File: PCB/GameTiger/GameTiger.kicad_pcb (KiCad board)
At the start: 2 copper layers, 81.3 x 99.8 mm, 79 parts, among them J1 USB TypeC Connector, J2 503398-1892, J3 LCD Display, J4 Speaker, Q1 DMG3415, U1 RP2040, U2 MCP73831-2-OT, U3 W25Q128JVSIQ, U4 PAM8302A, U5 AP2112K-3.3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

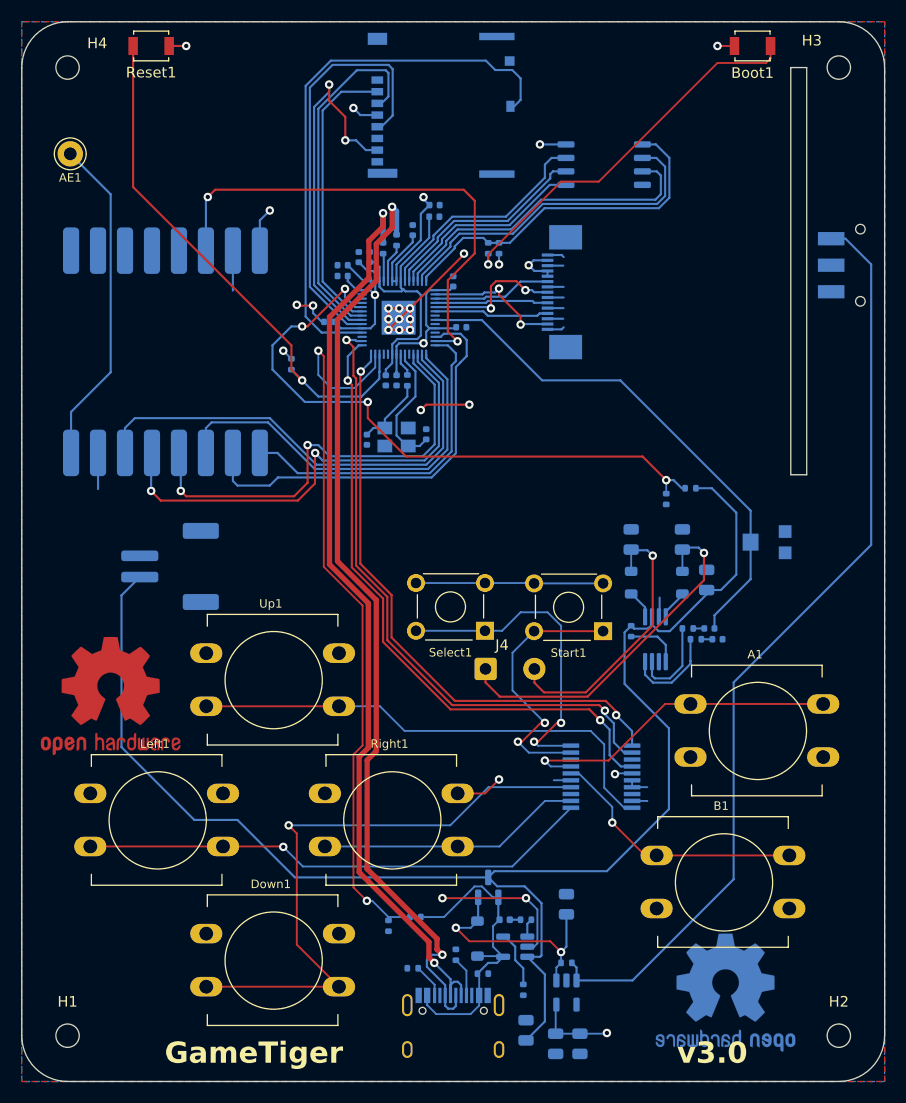
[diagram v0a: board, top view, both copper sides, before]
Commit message: Fixed differential pairs for USB-C connection
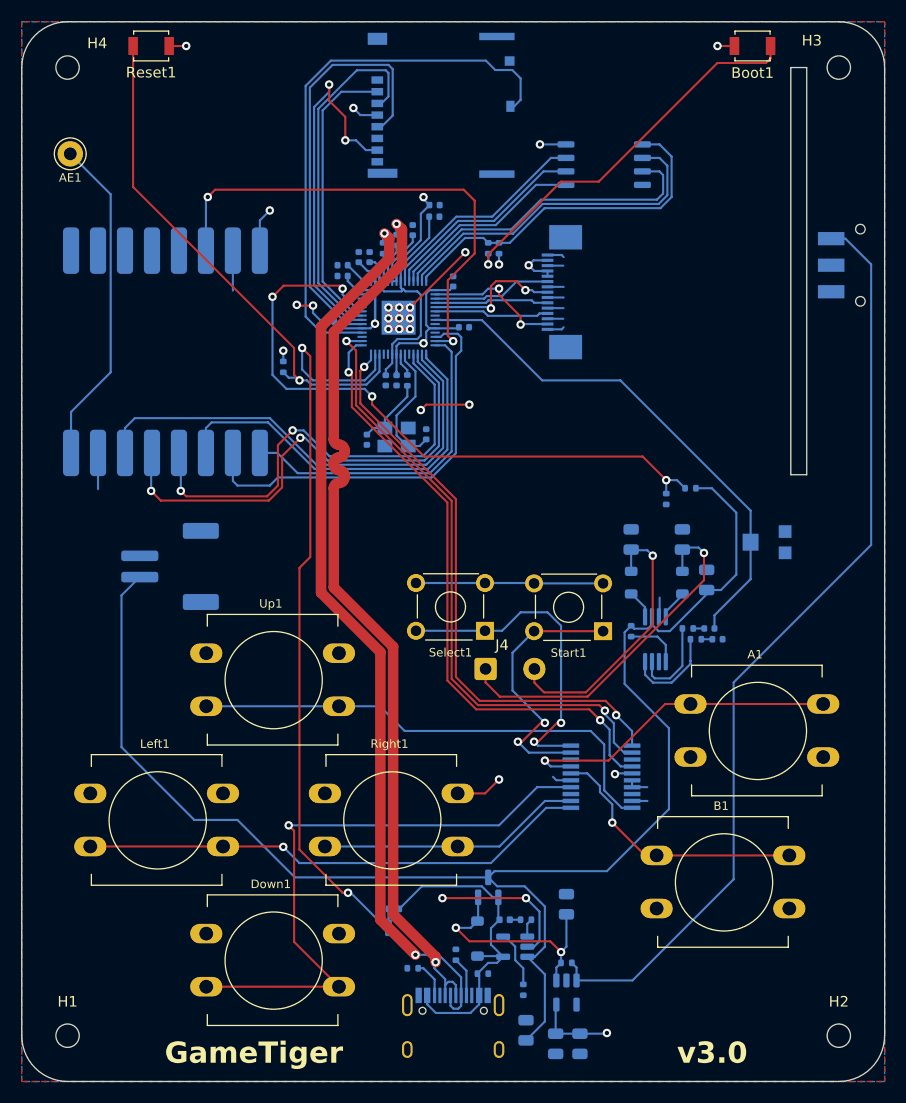
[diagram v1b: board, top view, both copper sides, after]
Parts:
- removed REF** (x2): OSHW-Logo2_14.6x12mm_Copper, Symbol:OSHW-Logo2_14.6x12mm_Copper
- U3: footprint Package_SO:SOIC-8_5.23x5.23mm_P1.27mm -> Package_SO:SOP-8_5.28x5.23mm_P1.27mm
- moved R19 2.17 mm to (70.6, 119.4)
- moved R16 0.80 mm to (60.2, 68.3)
- moved C8 0.25 mm to (77.2, 64.6)
- moved R20 0.19 mm to (70.1, 121.2)
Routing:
- net POWER_USB_DP: track 89.1 -> 85.4 mm
- net BATTERY_LVL: track 59.1 -> 62.4 mm
- net POWER_DETECT: track 69.0 -> 71.7 mm
- net +3.3V: track 73.5 -> 76.1 mm
- net VBUS: track 29.7 -> 31.5 mm
- net POWER_USB_DN: track 87.2 -> 85.5 mm
- net KYBD_SCL: track 60.1 -> 58.5 mm
- net KYBD_INT: track 56.2 -> 54.8 mm
- net KYBD_SDA: track 59.8 -> 58.4 mm
- net SX1262_CLK: track 45.0 -> 46.1 mm
- net GND: track 90.5 -> 91.5 mm
- net SX1262_MOSI: track 42.1 -> 43.1 mm
- net Flash_QSPI_SD3: track 21.6 -> 20.7 mm
- net Net-(U1-RUN): track 50.4 -> 49.7 mm
- net KYBD_B: track 24.6 -> 24.0 mm
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
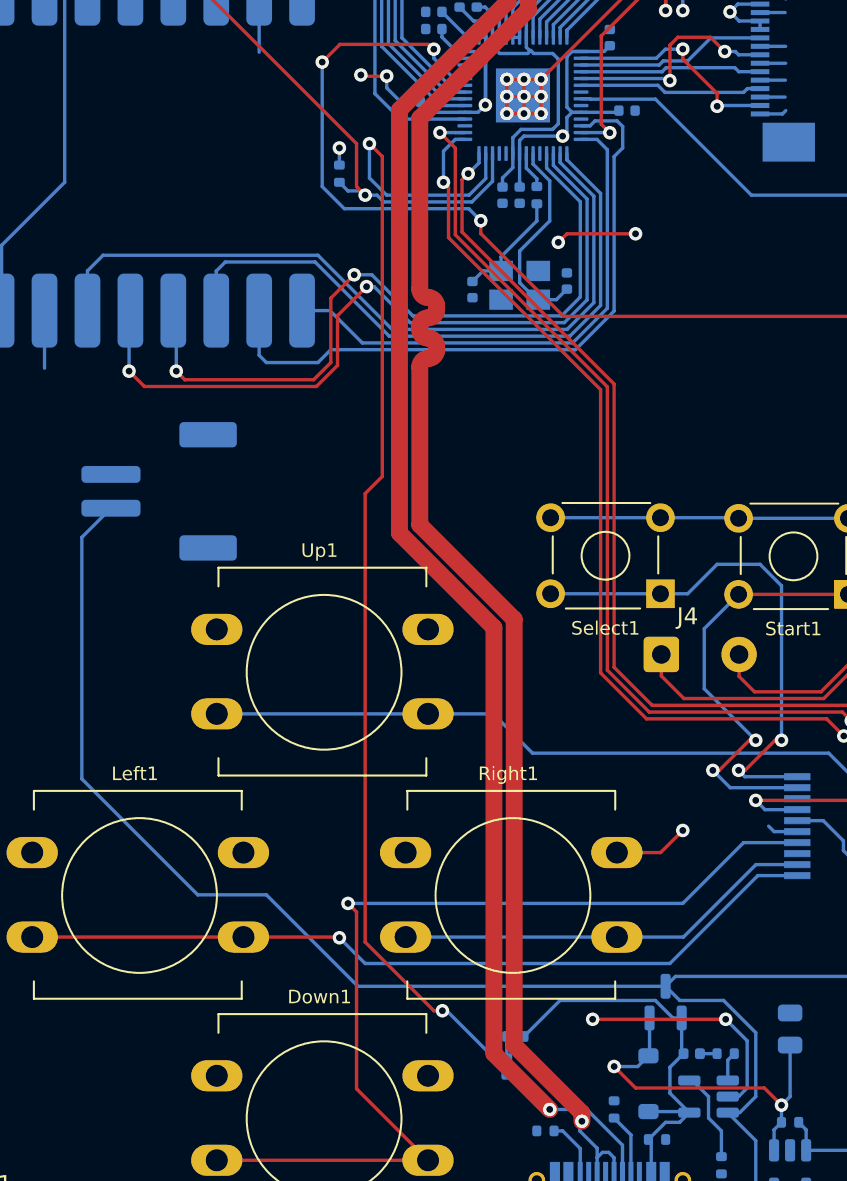
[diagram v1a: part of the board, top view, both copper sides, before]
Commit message: Updated PCB design with some improvements in differential pair for USB
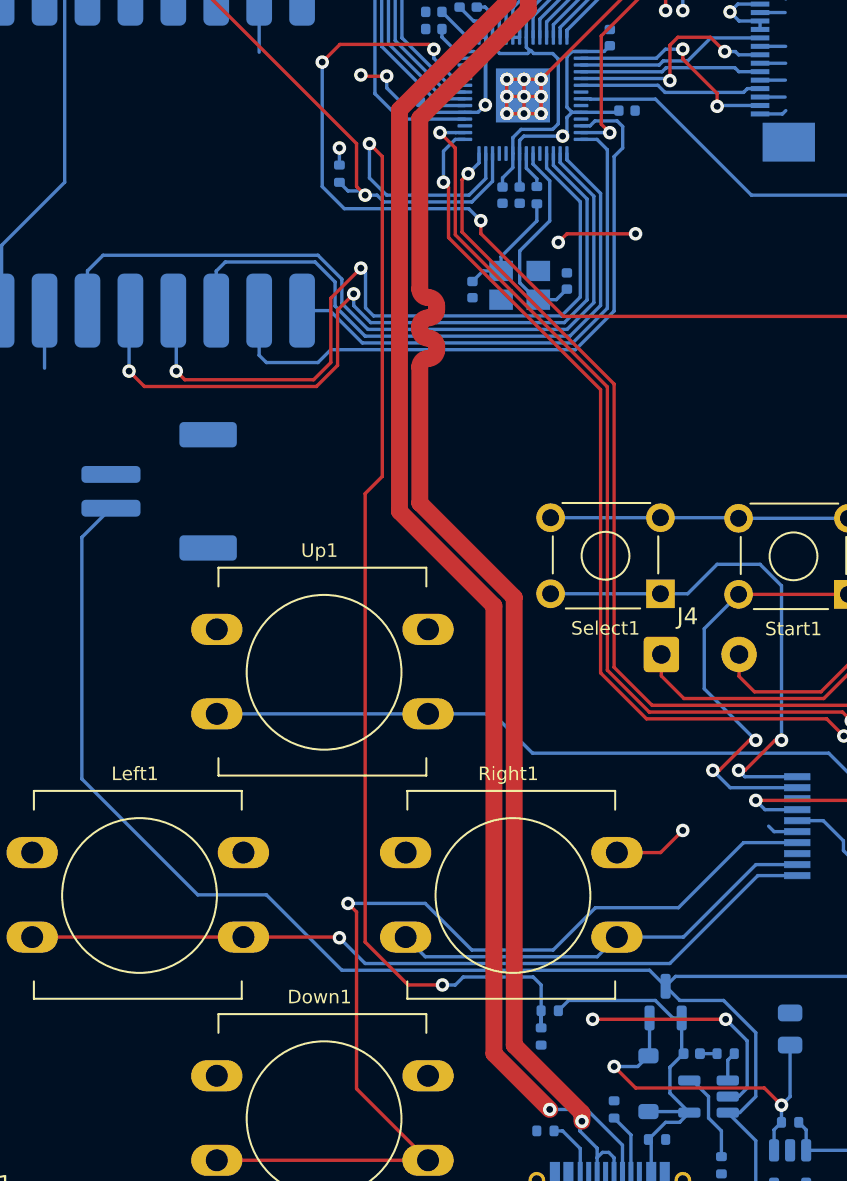
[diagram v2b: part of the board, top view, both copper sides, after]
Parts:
- moved R20 2.70 mm to (72.1, 119.4)
- moved R19 2.54 mm to (72.6, 117.9)
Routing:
- net POWER_DETECT: track 71.7 -> 74.6 mm
- net VBUS: track 31.5 -> 28.8 mm
- net KYBD_DOWN: track 57.7 -> 60.0 mm
- net SX1262_MOSI: track 43.1 -> 44.7 mm
- net KYBD_RIGHT: track 24.9 -> 25.9 mm
- net SX1262_MISO: track 37.7 -> 38.5 mm
- net SX1262_CS: track 44.8 -> 45.7 mm

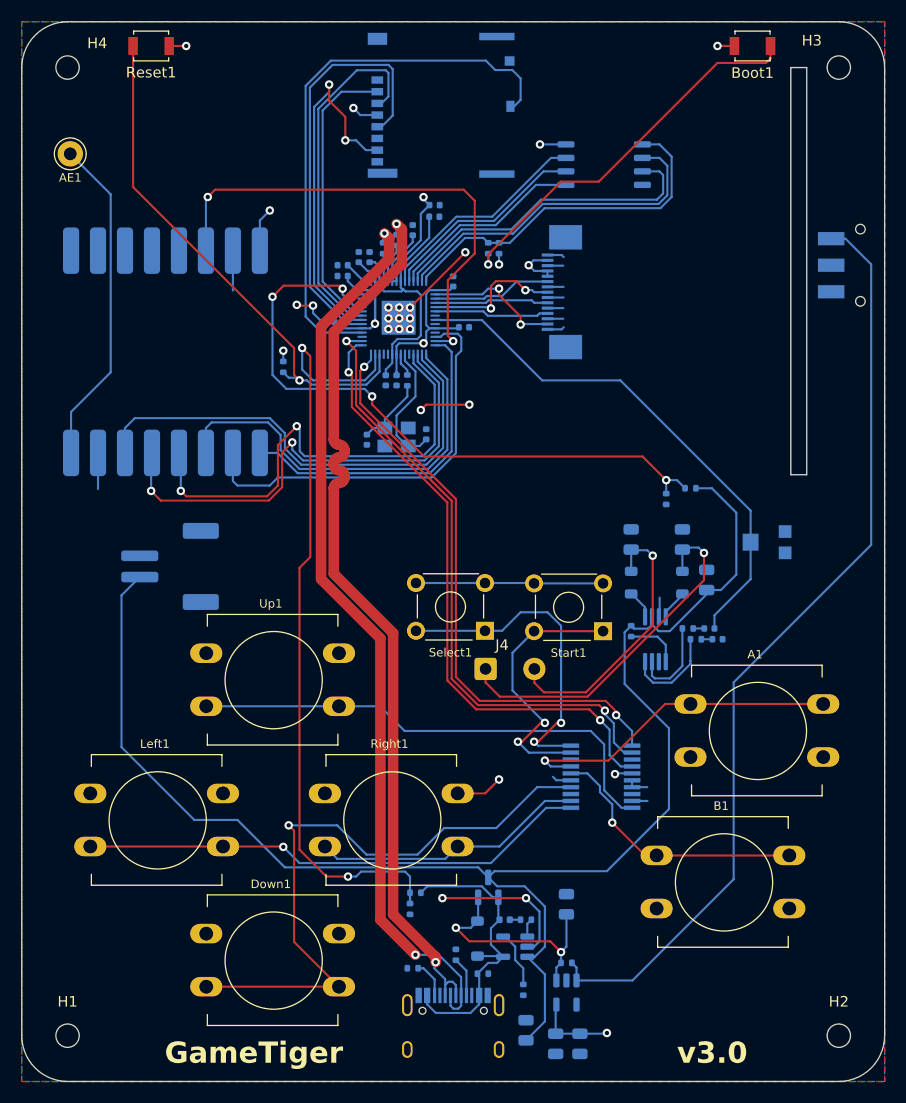
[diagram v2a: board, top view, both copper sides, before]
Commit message: Redesigned pcb layout to fix errors in decoupling caps and ground plane
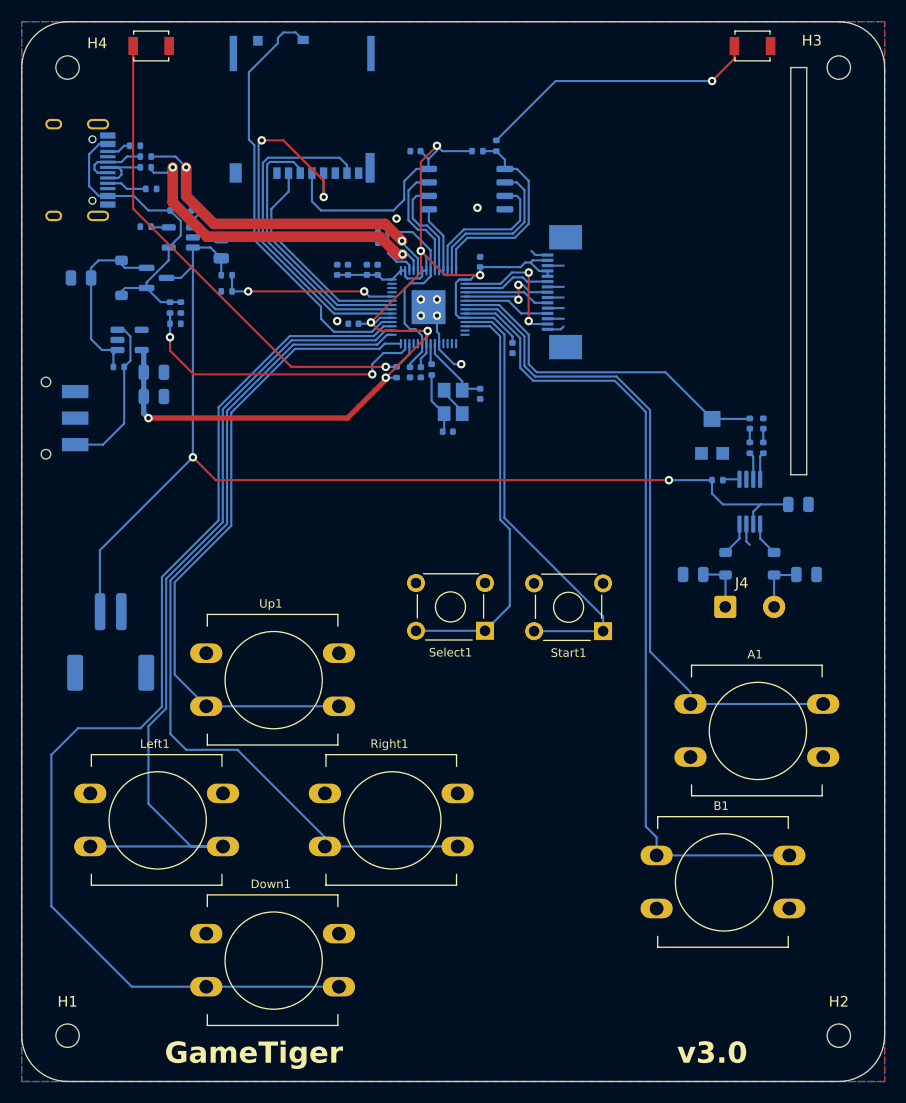
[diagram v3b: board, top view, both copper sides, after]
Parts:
- removed AE1: Antenna, Connector_Pin:Pin_D1.0mm_L10.0mm_LooseFit
- removed U6: PCF8574TS, PCF8574TS:SOP65P640X150-20N
- removed U7: ~, Waveshare:Core SX1262
- Boot1: value SW_Push -> Boot
- Reset1: value SW_Push -> Reset
- U3: value W25Q128JVSIQ -> W25Q64JVSSIQ; footprint Package_SO:SOP-8_5.28x5.23mm_P1.27mm -> Package_SO:SOIC-8_5.23x5.23mm_P1.27mm
- moved J1 89.6 mm to (39.6, 49.8), turned to 90 degrees
- moved R21 81.8 mm to (46.2, 47.5), turned to 0 degrees
- moved R11 80.2 mm to (47.2, 55.1), turned to 180 degrees
- moved C4 79.1 mm to (54.4, 57.1)
- moved Power1 78.0 mm to (37.8, 73.2), turned to 90 degrees
- moved R22 77.6 mm to (47.8, 51.6), turned to 0 degrees
- moved C1 74.6 mm to (41.1, 59.9), turned to 180 degrees
- moved U5 74.0 mm to (45.7, 65.8), turned to 0 degrees
- moved U2 73.9 mm to (50.5, 56.1)
- moved C19 73.7 mm to (48.0, 68.8), turned to 180 degrees
- moved D2 73.6 mm to (50.0, 53.6)
- moved R13 73.6 mm to (52.1, 53.6)
- moved C23 73.0 mm to (48.0, 71.1), turned to 180 degrees
- moved D1 70.7 mm to (45.0, 59.9)
- moved R12 70.2 mm to (44.7, 68.3)
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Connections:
- U1 pad 11: unconnected-(U1-GPIO8-Pad11) -> KYBD_START
- U1 pad 12: SX1262_RESET -> KYBD_SELECT
- U1 pad 13: SX1262_DIO1 -> unconnected-(U1-GPIO10-Pad13)
- U1 pad 14: SX1262_BUSY -> unconnected-(U1-GPIO11-Pad14)
- U1 pad 15: SX1262_MISO -> unconnected-(U1-GPIO12-Pad15)
- U1 pad 16: SX1262_CS -> unconnected-(U1-GPIO13-Pad16)
- U1 pad 17: SX1262_CLK -> unconnected-(U1-GPIO14-Pad17)
- U1 pad 18: SX1262_MOSI -> unconnected-(U1-GPIO15-Pad18)
- U1 pad 19: unconnected-(U1-TESTEN-Pad19) -> GND
- U1 pad 28: KYBD_INT -> KYBD_UP
- U1 pad 29: KYBD_SDA -> KYBD_RIGHT
- U1 pad 30: KYBD_SCL -> KYBD_LEFT
- U1 pad 31: unconnected-(U1-GPIO20-Pad31) -> KYBD_DOWN
- U1 pad 7: unconnected-(U1-GPIO5-Pad7) -> Audio_PWM
- U1 pad 8: Audio_PWM -> KYBD_A
- U1 pad 9: unconnected-(U1-GPIO7-Pad9) -> KYBD_B
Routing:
- net POWER_USB_DN: track 85.5 -> 6.28 mm, vias 2 -> 0
- net POWER_USB_DP: track 85.4 -> 6.46 mm, vias 2 -> 0
- net EN: track 88.6 -> 15.4 mm
- net GND: track 91.5 -> 21.9 mm, vias 19 -> 8
- net KYBD_SCL: track 58.5 -> 0.00 mm, vias 2 -> 0
- net KYBD_SDA: track 58.4 -> 0.00 mm, vias 2 -> 0
- net +3.3V: track 76.1 -> 134.4 mm, vias 11 -> 7
- net KYBD_RIGHT: track 25.9 -> 83.1 mm
- net KYBD_INT: track 54.8 -> 0.00 mm, vias 2 -> 0
- net KYBD_B: track 24.0 -> 77.2 mm, vias 1 -> 0
- net SX1262_DIO1: track 47.2 -> 0.00 mm, vias 2 -> 0
- net KYBD_DOWN: track 60.0 -> 106.7 mm, vias 1 -> 0
- net SX1262_CLK: track 46.3 -> 0.00 mm, vias 2 -> 0
- net POWER_DETECT: track 74.6 -> 28.7 mm
- net SX1262_CS: track 45.7 -> 0.00 mm
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- added copper zone on F.Cu, net GND
- removed copper zone on F.Cu, net +3.3V

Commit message: PCB Design track cleanup
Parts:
- removed H1, H2, H3, H4: MountingHole, MountingHole:MountingHole_2.2mm_M2
- added REF**: OSHW-Logo2_14.6x12mm_SilkScreen, Symbol:OSHW-Logo2_14.6x12mm_SilkScreen, F.Cu at (81.3, 125.5)
- A1: value SW_Push -> A
- B1: value SW_Push -> B
- Down1: value SW_Push -> Down
- Left1: value SW_Push -> Left
- Power1: value SW_Push -> Power
- Right1: value SW_Push -> Right
- Select1: value SW_Push -> Select
- Start1: value SW_Push -> Start
- Up1: value SW_Push -> Up
- moved R7 10.9 mm to (90.4, 78.5)
- moved B1 6.70 mm to (90.4, 118.9)
- moved Select1 6.65 mm to (79.5, 99.8)
- moved Start1 6.60 mm to (90.4, 99.8)
- moved C15 5.76 mm to (70.6, 55.4), turned to 180 degrees
- moved J3 5.36 mm to (89.4, 65.8)
- moved J4 4.32 mm to (101.9, 95.2)
- moved C12 3.45 mm to (68.6, 58.2), turned to 180 degrees
- moved A1 3.06 mm to (98.3, 103.1)
- moved C10 2.88 mm to (79.5, 64.8)
- moved Left1 2.76 mm to (41.9, 111.3)
- moved Down1 2.75 mm to (52.9, 124.5)
- moved Right1 2.75 mm to (64.1, 111.3)
- moved Up1 2.75 mm to (52.9, 98.0)
- moved C17 2.34 mm to (102.4, 75.2), turned to 180 degrees
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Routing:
- net +3.3V: track 134.4 -> 144.5 mm
- net GND: track 21.9 -> 27.9 mm, vias 8 -> 10
- net KYBD_RIGHT: track 83.1 -> 88.8 mm
- net LCD_RESET: track 8.27 -> 13.8 mm
- net KYBD_SELECT: track 39.3 -> 44.8 mm
- net Audio_PWM: track 32.9 -> 38.3 mm
- net LCD_DC: track 12.9 -> 18.0 mm
- net Net-(J4-Pin_2): track 5.12 -> 10.0 mm
- net Net-(J4-Pin_1): track 5.13 -> 10.0 mm
- net LCD_CLK: track 8.19 -> 13.0 mm
- net LCD_DATA: track 9.59 -> 13.7 mm
- net LCD_CS: track 8.35 -> 12.3 mm
- net KYBD_START: track 42.5 -> 45.4 mm
- net KYBD_UP: track 62.3 -> 65.0 mm
- net KYBD_DOWN: track 106.7 -> 108.7 mm
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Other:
- outline, holes or cut-outs redrawn
- board text removed: "v3.0"
